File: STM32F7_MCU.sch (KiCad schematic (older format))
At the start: 49 parts, among them IC4 STM32F769IIT6, IC5 LD1117ADT33TR, Y1 25MHz, Y2 XTAL016178-85SMX

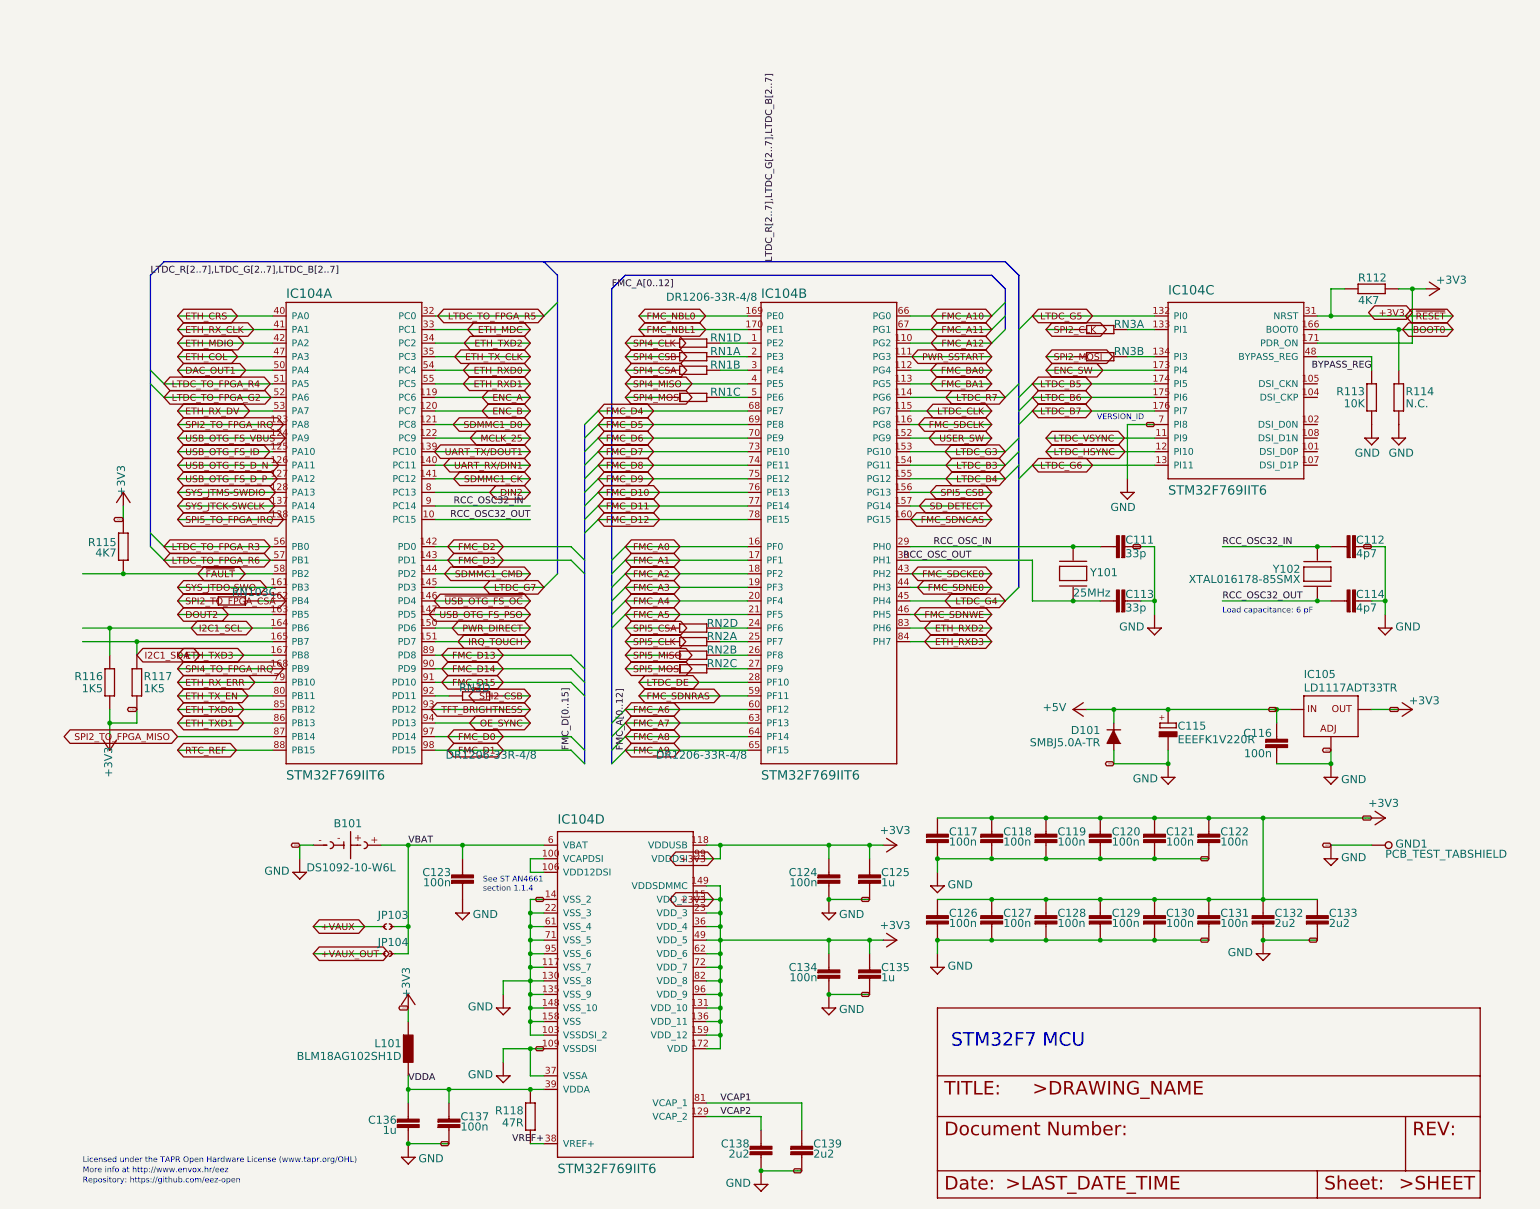
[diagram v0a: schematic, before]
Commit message: Adding TO FROM FPGA lines
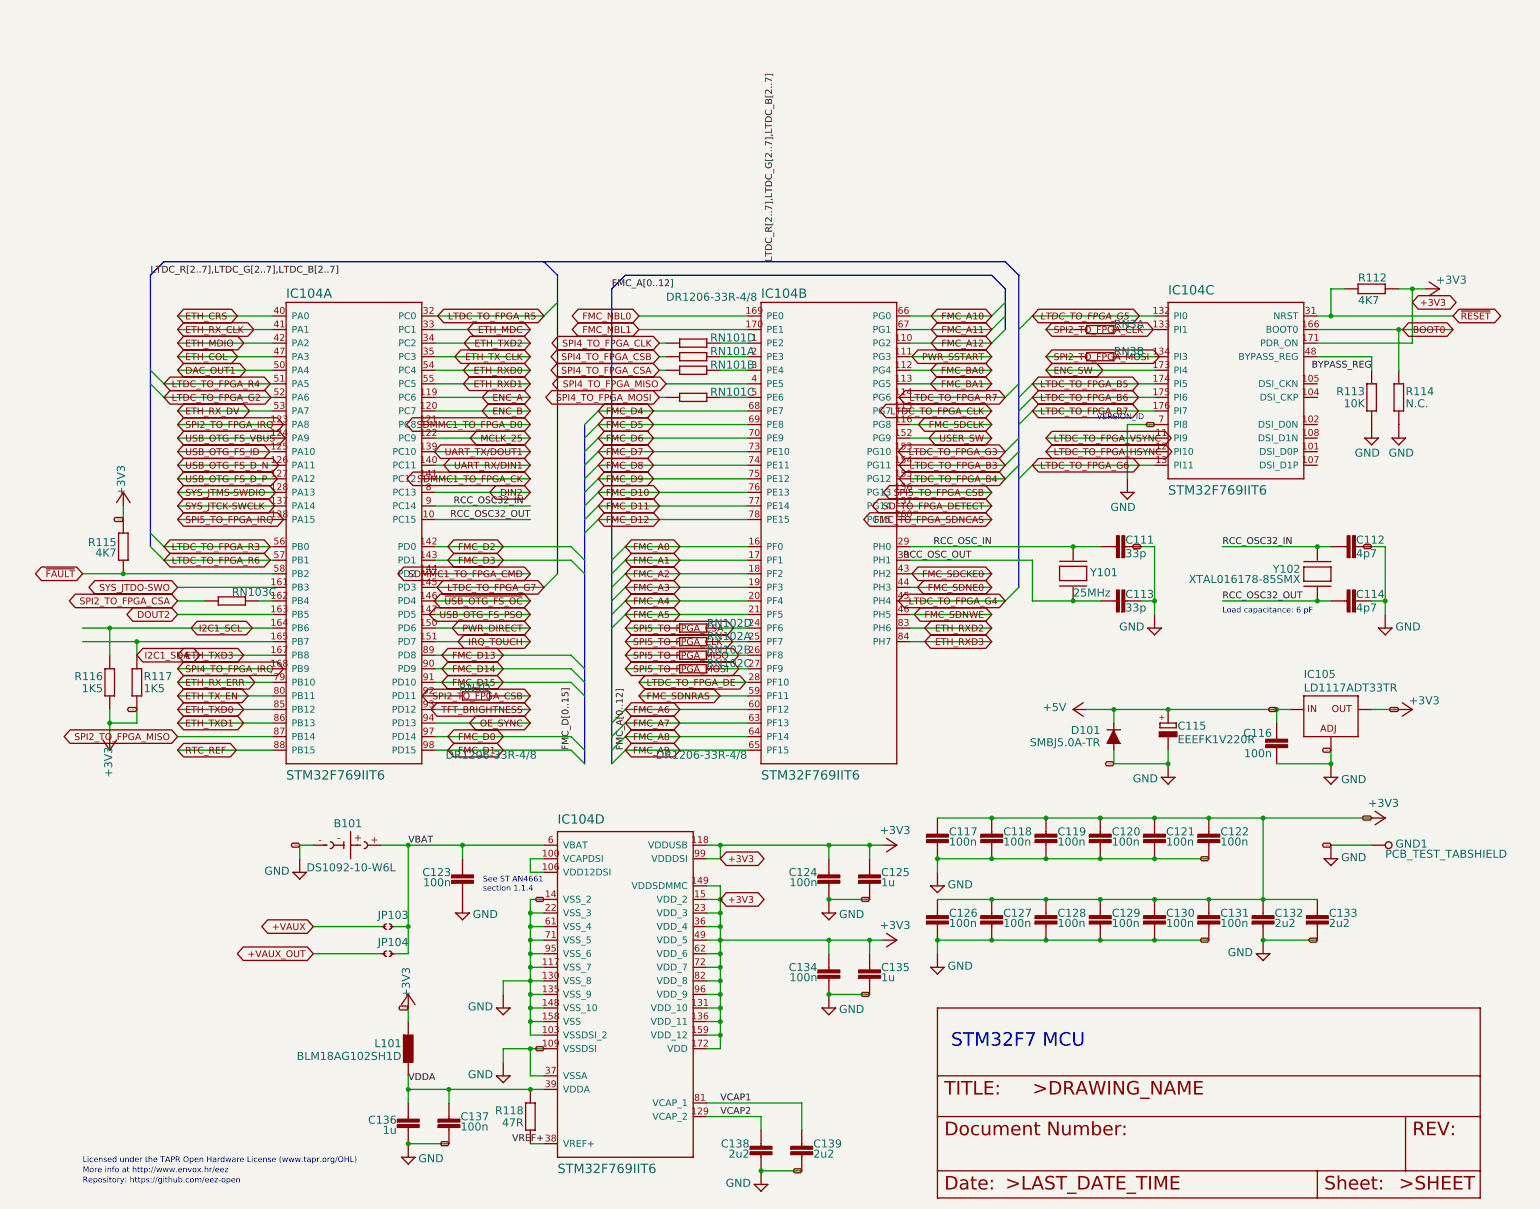
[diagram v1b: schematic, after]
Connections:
- net FMC_SDNCAS renamed FMC_TO_FPGA_SDNCAS
- net LTDC_B3 renamed LTDC_TO_FPGA_B3
- net LTDC_B4 renamed LTDC_TO_FPGA_B4
- net LTDC_B5 renamed LTDC_TO_FPGA_B5
- net LTDC_B6 renamed LTDC_TO_FPGA_B6
- net LTDC_B7 renamed LTDC_TO_FPGA_B7
- net LTDC_CLK renamed LTDC_TO_FPGA_CLK
- net LTDC_DE renamed LTDC_TO_FPGA_DE
- net LTDC_G3 renamed LTDC_TO_FPGA_G3
- net LTDC_G4 renamed LTDC_TO_FPGA_G4
- net LTDC_G5 renamed LTDC_TO_FPGA_G5
- net LTDC_G6 renamed LTDC_TO_FPGA_G6
- net LTDC_G7 renamed LTDC_TO_FPGA_G7
- net LTDC_HSYNC renamed LTDC_TO_FPGA_HSYNC
- net LTDC_R7 renamed LTDC_TO_FPGA_R7
- net LTDC_VSYNC renamed LTDC_TO_FPGA_VSYNC
- net SDMMC1_CK renamed SDMMC1_TO_FPGA_CK
- net SDMMC1_CMD renamed SDMMC1_TO_FPGA_CMD
- net SDMMC1_D0 renamed SDMMC1_TO_FPGA_D0
- net SD_DETECT renamed SD_TO_FPGA_DETECT
- net SPI2_CLK renamed SPI2_TO_FPGA_CLK
- net SPI2_CSB renamed SPI2_TO_FPGA_CSB
- net SPI2_MOSI renamed SPI2_TO_FPGA_MOSI
- net SPI4_CLK renamed SPI4_TO_FPGA_CLK
- net SPI4_CSA renamed SPI4_TO_FPGA_CSA
- net SPI4_CSB renamed SPI4_TO_FPGA_CSB
- net SPI4_MISO renamed SPI4_TO_FPGA_MISO
- net SPI4_MOSI renamed SPI4_TO_FPGA_MOSI
- net SPI5_CLK renamed SPI5_TO_FPGA_CLK
- net SPI5_CSA renamed SPI5_TO_FPGA_CSA
- net SPI5_CSB renamed SPI5_TO_FPGA_CSB
- net SPI5_MISO renamed SPI5_TO_FPGA_MISO
- net SPI5_MOSI renamed SPI5_TO_FPGA_MOSI
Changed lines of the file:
@@
 Wire Wire Line
 	2400 4600 1700 4600
-Text GLabel 1700 4600 2    50   BiDi ~ 0
+Text GLabel 1700 4600 0    50   BiDi ~ 0
 SYS_JTDO-SWO
 Wire Wire Line
@@
 	3600 3400 4300 3400
 Text GLabel 4300 3400 0    50   BiDi ~ 0
-SDMMC1_D0
+SDMMC1_TO_FPGA_D0
 Wire Wire Line
 	3600 3500 4300 3500
@@
 	3600 3800 4300 3800
 Text GLabel 4300 3800 0    50   BiDi ~ 0
-SDMMC1_CK
+SDMMC1_TO_FPGA_CK
 Wire Wire Line
 	3600 3900 4300 3900
@@
 Wire Wire Line
 	2400 4800 1700 4800
-Text GLabel 1700 4800 2    50   BiDi ~ 0
+Text GLabel 1700 4800 0    50   BiDi ~ 0
 DOUT2
 Wire Wire Line
 	3600 4500 4300 4500
 Text GLabel 4300 4500 0    50   BiDi ~ 0
-SDMMC1_CMD
+SDMMC1_TO_FPGA_CMD
 Wire Wire Line
 	3600 5600 4300 5600
@@
 Wire Wire Line
 	5900 2600 5100 2600
-Text GLabel 5100 2600 2    50   BiDi ~ 0
+Text GLabel 5100 2600 0    50   BiDi ~ 0
 FMC_NBL0
 Wire Wire Line
@@
 Wire Wire Line
 	10200 2400 10200 2600
-Text GLabel 11100 2600 0    50   BiDi ~ 0
+Text GLabel 11100 2600 2    50   BiDi ~ 0
 ~RESET
 Connection ~ 10200 2600
@@
 Wire Wire Line
 	5900 2700 5100 2700
-Text GLabel 5100 2700 2    50   BiDi ~ 0
+Text GLabel 5100 2700 0    50   BiDi ~ 0
 FMC_NBL1
 Wire Wire Line
@@
 	7100 4000 7700 4000
 Text GLabel 7700 4000 0    50   BiDi ~ 0
-SD_DETECT
+SD_TO_FPGA_DETECT
 Wire Wire Line
 	5300 5000 5000 5000
 Text GLabel 5000 5000 2    50   BiDi ~ 0
-SPI5_CLK
+SPI5_TO_FPGA_CLK
 Wire Wire Line
 	5300 5100 5000 5100
 Text GLabel 5000 5100 2    50   BiDi ~ 0
-SPI5_MISO
+SPI5_TO_FPGA_MISO
 Wire Wire Line
 	5300 5200 5000 5200
 Text GLabel 5000 5200 2    50   BiDi ~ 0
-SPI5_MOSI
+SPI5_TO_FPGA_MOSI
 Wire Wire Line
 	5900 5300 5100 5300
 Text GLabel 5100 5300 2    50   BiDi ~ 0
-LTDC_DE
+LTDC_TO_FPGA_DE
 Wire Wire Line
 	5900 5400 5100 5400
@@
 	7100 3300 7700 3300
 Text GLabel 7700 3300 0    50   BiDi ~ 0
-LTDC_CLK
+LTDC_TO_FPGA_CLK
 Wire Wire Line
 	7100 3400 7700 3400
@@
 	7100 4100 7700 4100
 Text GLabel 7700 4100 0    50   BiDi ~ 0
-FMC_SDNCAS
+FMC_TO_FPGA_SDNCAS
 Wire Wire Line
 	7100 4300 8300 4300
@@
 	7100 4700 7800 4700
 Text GLabel 7800 4700 0    50   BiDi ~ 0
-LTDC_G4
+LTDC_TO_FPGA_G4
 Wire Wire Line
 	7100 4800 7700 4800
@@
 	8300 2700 8100 2700
 Text GLabel 8100 2700 2    50   BiDi ~ 0
-SPI2_CLK
+SPI2_TO_FPGA_CLK
 Wire Wire Line
 	8300 2900 8100 2900
 Text GLabel 8100 2900 2    50   BiDi ~ 0
-SPI2_MOSI
+SPI2_TO_FPGA_MOSI
 Wire Wire Line
 	8900 3000 8100 3000
@@
 	8900 3500 8100 3500
 Text GLabel 8100 3500 2    50   BiDi ~ 0
-LTDC_VSYNC
+LTDC_TO_FPGA_VSYNC
 Wire Wire Line
 	8900 3600 8100 3600
 Text GLabel 8100 3600 2    50   BiDi ~ 0
-LTDC_HSYNC
+LTDC_TO_FPGA_HSYNC
 Wire Wire Line
 	8900 3700 8000 3700
 Text GLabel 8000 3700 2    50   BiDi ~ 0
-LTDC_G6
+LTDC_TO_FPGA_G6
 Wire Wire Line
 	10100 2700 10700 2700
@@
 	7100 3200 7800 3200
 Text GLabel 7800 3200 0    50   BiDi ~ 0
-LTDC_R7
+LTDC_TO_FPGA_R7
 Wire Wire Line
 	8900 2600 8000 2600
-Text GLabel 8000 2600 2    50   BiDi ~ 0
-LTDC_G5
+Text GLabel 8000 2600 2    50   BiDi Italic 0
+LTDC_TO_FPGA_G5
 Wire Wire Line
 	4600 4300 3600 4300
@@
 	3600 4600 4400 4600
 Text GLabel 4400 4600 0    50   BiDi ~ 0
-LTDC_G7
+LTDC_TO_FPGA_G7
 Wire Wire Line
 	7100 3600 7800 3600
 Text GLabel 7800 3600 0    50   BiDi ~ 0
-LTDC_G3
+LTDC_TO_FPGA_G3
 Wire Wire Line
 	7100 3700 7800 3700
 Text GLabel 7800 3700 0    50   BiDi ~ 0
-LTDC_B3
+LTDC_TO_FPGA_B3
 Wire Wire Line
 	7100 3800 7800 3800
 Text GLabel 7800 3800 0    50   BiDi ~ 0
-LTDC_B4
+LTDC_TO_FPGA_B4
 Wire Wire Line
 	8900 3100 8000 3100
 Text GLabel 8000 3100 2    50   BiDi ~ 0
-LTDC_B5
+LTDC_TO_FPGA_B5
 Wire Wire Line
 	8900 3200 8000 3200
 Text GLabel 8000 3200 2    50   BiDi ~ 0
-LTDC_B6
+LTDC_TO_FPGA_B6
 Wire Wire Line
 	8900 3300 8000 3300
 Text GLabel 8000 3300 2    50   BiDi ~ 0
-LTDC_B7
+LTDC_TO_FPGA_B7
 Wire Wire Line
 	9300 6600 8900 6600
@@
 	6500 7200 5700 7200
 Connection ~ 6500 7200
-Text GLabel 5650 6900 0    50   BiDi ~ 0
+Text GLabel 5700 6900 2    50   BiDi ~ 0
 +3V3
 Connection ~ 6800 7200
@@
 Wire Wire Line
 	5700 6600 5700 6500
-Text GLabel 5650 6600 0    50   BiDi ~ 0
+Text GLabel 5700 6600 2    50   BiDi ~ 0
 +3V3
 Connection ~ 6500 6500
@@
 Wire Wire Line
 	10800 2400 10900 2400
-Text GLabel 10800 2575 0    50   BiDi ~ 0
+Text GLabel 10800 2500 2    50   BiDi ~ 0
 +3V3
 Connection ~ 10800 2400
@@
 Text GLabel 4300 5000 0    50   BiDi ~ 0
 IRQ_TOUCH
-Wire Wire Line
-	5300 2800 5000 2800
-Text GLabel 5000 2800 2    50   BiDi ~ 0
-SPI4_CLK
-Wire Wire Line
-	5900 3100 5000 3100
-Text GLabel 5000 3100 2    50   BiDi ~ 0
-SPI4_MISO
-Wire Wire Line
-	5300 3200 5000 3200
-Text GLabel 5000 3200 2    50   BiDi ~ 0
-SPI4_MOSI
+Text GLabel 5250 2800 0    50   BiDi ~ 0
+SPI4_TO_FPGA_CLK
+Text GLabel 5300 3100 0    50   BiDi ~ 0
+SPI4_TO_FPGA_MISO
+Text GLabel 5250 3200 0    50   BiDi ~ 0
+SPI4_TO_FPGA_MOSI
 Wire Wire Line
 	7100 3900 7700 3900
 Text GLabel 7700 3900 0    50   BiDi ~ 0
-SPI5_CSB
+SPI5_TO_FPGA_CSB
 Wire Wire Line
 	5300 4900 5000 4900
 Text GLabel 5000 4900 2    50   BiDi ~ 0
-SPI5_CSA
+SPI5_TO_FPGA_CSA
 Wire Wire Line
 	2400 4500 1300 4500
 Wire Wire Line
 	1300 4500 1000 4500
-Text GLabel 1850 4500 2    50   BiDi ~ 0
+Text GLabel 1000 4500 0    50   BiDi ~ 0
 ~FAULT
 Connection ~ 1300 4500
@@
 Wire Wire Line
 	3200 7100 2700 7100
-Text GLabel 2700 7100 2    50   BiDi ~ 0
+Text GLabel 2700 7100 0    50   BiDi ~ 0
 +VAUX
-Wire Wire Line
-	5000 2900 5300 2900
-Text GLabel 5000 2900 2    50   BiDi ~ 0
-SPI4_CSB
-Wire Wire Line
-	5000 3000 5300 3000
-Text GLabel 5000 3000 2    50   BiDi ~ 0
-SPI4_CSA
+Text GLabel 5250 2900 0    50   BiDi ~ 0
+SPI4_TO_FPGA_CSB
+Text GLabel 5250 3000 0    50   BiDi ~ 0
+SPI4_TO_FPGA_CSA
 Wire Wire Line
 	4100 5400 4300 5400
 Text GLabel 4300 5400 0    50   BiDi ~ 0
-SPI2_CSB
+SPI2_TO_FPGA_CSB
 Wire Wire Line
 	1900 4700 1700 4700
-Text GLabel 1700 4700 2    50   BiDi ~ 0
+Text GLabel 1700 4700 0    50   BiDi ~ 0
 SPI2_TO_FPGA_CSA
 Wire Wire Line
@@
 Wire Wire Line
 	3200 7300 2700 7300
-Text GLabel 2700 7300 2    50   BiDi ~ 0
+Text GLabel 2700 7300 0    50   BiDi ~ 0
 +VAUX_OUT
 Wire Wire Line
@@
 AR Path="/5F88D05D/112503EE965A383E" Ref="RN2"  Part="1"
 AR Path="/5F88BD9A/112503EE965A383E" Ref="RN2"  Part="1"
-AR Path="/5F88BD9A/965A383E" Ref="RN2"  Part="1"
-F 0 "RN2" H 5600 5005 59  0000 L BNN
+AR Path="/5F88BD9A/965A383E" Ref="RN102"  Part="1"
+F 0 "RN102" H 5600 5005 59  0000 L BNN
 F 1 "DR1206-33R-4/8" H 5600 4880 59  0001 L BNN
 F 2 "EEZ DIB MCU r3B4:CAY16" H 5500 5000 50  0001 C CNN
@@
 AR Path="/5F88D05D/112503EE965A3832" Ref="RN2"  Part="2"
 AR Path="/5F88BD9A/112503EE965A3832" Ref="RN2"  Part="2"
-AR Path="/5F88BD9A/965A3832" Ref="RN2"  Part="2"
-F 0 "RN2" H 5600 5105 59  0000 L BNN
+AR Path="/5F88BD9A/965A3832" Ref="RN102"  Part="2"
+F 0 "RN102" H 5600 5105 59  0000 L BNN
 F 1 "DR1206-33R-4/8" H 5600 4980 59  0001 L BNN
 F 2 "EEZ DIB MCU r3B4:CAY16" H 5500 5100 50  0001 C CNN
@@
 AR Path="/5F88D05D/112503EE965A3836" Ref="RN2"  Part="3"
 AR Path="/5F88BD9A/112503EE965A3836" Ref="RN2"  Part="3"
-AR Path="/5F88BD9A/965A3836" Ref="RN2"  Part="3"
-F 0 "RN2" H 5600 5205 59  0000 L BNN
+AR Path="/5F88BD9A/965A3836" Ref="RN102"  Part="3"
+F 0 "RN102" H 5600 5205 59  0000 L BNN
 F 1 "DR1206-33R-4/8" H 5600 5080 59  0001 L BNN
 F 2 "EEZ DIB MCU r3B4:CAY16" H 5500 5200 50  0001 C CNN
@@
 AR Path="/5F88D05D/112503EE965A382A" Ref="RN2"  Part="4"
 AR Path="/5F88BD9A/112503EE965A382A" Ref="RN2"  Part="4"
-AR Path="/5F88BD9A/965A382A" Ref="RN2"  Part="4"
-F 0 "RN2" H 5600 4970 59  0000 L TNN
+AR Path="/5F88BD9A/965A382A" Ref="RN102"  Part="4"
+F 0 "RN102" H 5600 4970 59  0000 L TNN
 F 1 "DR1206-33R-4/8" H 5225 3930 59  0000 L BNN
 F 2 "EEZ DIB MCU r3B4:CAY16" H 5500 4900 50  0001 C CNN
@@
 AR Path="/5F88D05D/1745A48E69CE5986" Ref="RN1"  Part="1"
 AR Path="/5F88BD9A/1745A48E69CE5986" Ref="RN1"  Part="1"
-AR Path="/5F88BD9A/69CE5986" Ref="RN1"  Part="1"
-F 0 "RN1" H 5625 2905 59  0000 L BNN
+AR Path="/5F88BD9A/69CE5986" Ref="RN101"  Part="1"
+F 0 "RN101" H 5625 2905 59  0000 L BNN
 F 1 "DR1206-33R-4/8" H 5600 2780 59  0001 L BNN
 F 2 "EEZ DIB MCU r3B4:CAY16" H 5500 2900 50  0001 C CNN
@@
 AR Path="/5F88D05D/1745A48E69CE598A" Ref="RN1"  Part="2"
 AR Path="/5F88BD9A/1745A48E69CE598A" Ref="RN1"  Part="2"
-AR Path="/5F88BD9A/69CE598A" Ref="RN1"  Part="2"
-F 0 "RN1" H 5625 3005 59  0000 L BNN
+AR Path="/5F88BD9A/69CE598A" Ref="RN101"  Part="2"
+F 0 "RN101" H 5625 3005 59  0000 L BNN
 F 1 "DR1206-33R-4/8" H 5600 2880 59  0001 L BNN
 F 2 "EEZ DIB MCU r3B4:CAY16" H 5500 3000 50  0001 C CNN
@@
 AR Path="/5F88D05D/1745A48E69CE598E" Ref="RN1"  Part="3"
 AR Path="/5F88BD9A/1745A48E69CE598E" Ref="RN1"  Part="3"
-AR Path="/5F88BD9A/69CE598E" Ref="RN1"  Part="3"
-F 0 "RN1" H 5625 3205 59  0000 L BNN
+AR Path="/5F88BD9A/69CE598E" Ref="RN101"  Part="3"
+F 0 "RN101" H 5625 3205 59  0000 L BNN
 F 1 "DR1206-33R-4/8" H 5600 3080 59  0001 L BNN
 F 2 "EEZ DIB MCU r3B4:CAY16" H 5500 3200 50  0001 C CNN
@@
 AR Path="/5F88D05D/1745A48E69CE5992" Ref="RN1"  Part="4"
 AR Path="/5F88BD9A/1745A48E69CE5992" Ref="RN1"  Part="4"
-AR Path="/5F88BD9A/69CE5992" Ref="RN1"  Part="4"
-F 0 "RN1" H 5625 2805 59  0000 L BNN
+AR Path="/5F88BD9A/69CE5992" Ref="RN101"  Part="4"
+F 0 "RN101" H 5625 2805 59  0000 L BNN
 F 1 "DR1206-33R-4/8" H 5300 3105 59  0000 L BNN
 F 2 "EEZ DIB MCU r3B4:CAY16" H 5500 2800 50  0001 C CNN
@@
 Text Notes 8475 3375 0    42   ~ 0
 VERSION_ID
+Wire Wire Line
+	5250 2800 5300 2800
+Wire Wire Line
+	5250 2900 5300 2900
+Wire Wire Line
+	5250 3000 5300 3000
+Wire Wire Line
+	5300 3100 5900 3100
+Wire Wire Line
+	5250 3200 5300 3200
 Wire Bus Line
 	4500 2300 4500 4500

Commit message: Rewiering LCD OUT to bottom left
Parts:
- R12, R13, R14, R15: footprint Resistor_SMD:R_0805_2012Metric -> Resistor_SMD:R_0603_1608Metric
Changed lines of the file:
@@
 F 0 "R113" V 10509 3150 59  0000 R TNN
 F 1 "10K" V 10420 3150 59  0000 R TNN
-F 2 "Resistor_SMD:R_0805_2012Metric" H 10500 3200 50  0001 C CNN
+F 2 "Resistor_SMD:R_0603_1608Metric" H 10500 3200 50  0001 C CNN
 F 3 "" H 10500 3200 50  0001 C CNN
 	1    10500 3200
@@
 F 0 "R112" H 10600 2516 59  0000 R TNN
 F 1 "4K7" H 10600 2350 59  0000 R TNN
-F 2 "Resistor_SMD:R_0805_2012Metric" H 10500 2400 50  0001 C CNN
+F 2 "Resistor_SMD:R_0603_1608Metric" H 10500 2400 50  0001 C CNN
 F 3 "" H 10500 2400 50  0001 C CNN
 	1    10500 2400
@@
 F 0 "R115" V 1234 4350 59  0000 L TNN
 F 1 "4K7" V 1380 4350 59  0000 L BNN
-F 2 "Resistor_SMD:R_0805_2012Metric" H 1300 4300 50  0001 C CNN
+F 2 "Resistor_SMD:R_0603_1608Metric" H 1300 4300 50  0001 C CNN
 F 3 "" H 1300 4300 50  0001 C CNN
 	1    1300 4300
@@
 F 0 "R114" V 10709 3250 59  0000 L TNN
 F 1 "N.C." V 10620 3250 59  0000 L TNN
-F 2 "Resistor_SMD:R_0805_2012Metric" H 10700 3200 50  0001 C CNN
+F 2 "Resistor_SMD:R_0603_1608Metric" H 10700 3200 50  0001 C CNN
 F 3 "" H 10700 3200 50  0001 C CNN
 	1    10700 3200

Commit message: Update
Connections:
- net FMC_TO_FPGA_SDNCAS renamed FMC_SDNCAS
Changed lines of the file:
@@
 Wire Wire Line
 	7100 4000 7700 4000
-Text GLabel 7700 4000 0    50   BiDi ~ 0
+Text GLabel 7150 4000 2    50   BiDi ~ 0
 SD_TO_FPGA_DETECT
 Wire Wire Line
@@
 Text GLabel 5100 5400 2    50   BiDi ~ 0
 FMC_SDNRAS
-Wire Wire Line
-	7100 2900 7700 2900
-Text GLabel 7700 2900 0    50   BiDi ~ 0
+Text GLabel 7250 2900 2    50   BiDi ~ 0
 PWR_SSTART
-Wire Wire Line
-	7100 3000 7700 3000
-Text GLabel 7700 3000 0    50   BiDi ~ 0
+Text GLabel 7250 3000 2    50   BiDi ~ 0
 FMC_BA0
-Wire Wire Line
-	7100 3100 7700 3100
-Text GLabel 7700 3100 0    50   BiDi ~ 0
+Text GLabel 7250 3100 2    50   BiDi ~ 0
 FMC_BA1
 Wire Wire Line
 	7100 3300 7700 3300
-Text GLabel 7700 3300 0    50   BiDi ~ 0
+Text GLabel 7100 3300 2    50   BiDi ~ 0
 LTDC_TO_FPGA_CLK
 Wire Wire Line
@@
 	7100 4100 7700 4100
 Text GLabel 7700 4100 0    50   BiDi ~ 0
-FMC_TO_FPGA_SDNCAS
+FMC_SDNCAS
 Wire Wire Line
 	7100 4300 8300 4300
@@
 Wire Wire Line
 	8900 3700 8000 3700
-Text GLabel 8000 3700 2    50   BiDi ~ 0
+Text GLabel 8800 3700 0    50   BiDi ~ 0
 LTDC_TO_FPGA_G6
 Wire Wire Line
@@
 Text GLabel 7700 2600 0    50   BiDi ~ 0
 FMC_A10
-Wire Wire Line
-	7100 2700 7700 2700
 Text GLabel 7700 2700 0    50   BiDi ~ 0
 FMC_A11
@@
 Wire Wire Line
 	7100 3200 7800 3200
-Text GLabel 7800 3200 0    50   BiDi ~ 0
+Text GLabel 7150 3200 2    50   BiDi ~ 0
 LTDC_TO_FPGA_R7
 Wire Wire Line
@@
 Wire Wire Line
 	7100 3600 7800 3600
-Text GLabel 7800 3600 0    50   BiDi ~ 0
+Text GLabel 7150 3600 2    50   BiDi ~ 0
 LTDC_TO_FPGA_G3
 Wire Wire Line
 	7100 3700 7800 3700
-Text GLabel 7800 3700 0    50   BiDi ~ 0
+Text GLabel 7150 3700 2    50   BiDi ~ 0
 LTDC_TO_FPGA_B3
 Wire Wire Line
 	7100 3800 7800 3800
-Text GLabel 7800 3800 0    50   BiDi ~ 0
+Text GLabel 7150 3800 2    50   BiDi ~ 0
 LTDC_TO_FPGA_B4
 Wire Wire Line
@@
 Wire Wire Line
 	7100 3900 7700 3900
-Text GLabel 7700 3900 0    50   BiDi ~ 0
+Text GLabel 7150 3900 2    50   BiDi ~ 0
 SPI5_TO_FPGA_CSB
 Wire Wire Line
@@
 Text GLabel 4300 4900 0    50   BiDi ~ 0
 PWR_DIRECT
-Wire Wire Line
-	7700 2800 7100 2800
 Text GLabel 7700 2800 0    50   BiDi ~ 0
 FMC_A12
@@
 Wire Wire Line
 	5250 3200 5300 3200
+Wire Wire Line
+	7100 3100 7250 3100
+Wire Wire Line
+	7100 2700 7700 2700
+Wire Wire Line
+	7700 2800 7100 2800
+Wire Wire Line
+	7100 2900 7250 2900
+Wire Wire Line
+	7250 3000 7100 3000
 Wire Bus Line
 	4500 2300 4500 4500
